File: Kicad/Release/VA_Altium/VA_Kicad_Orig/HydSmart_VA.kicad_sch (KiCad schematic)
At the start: 0 parts

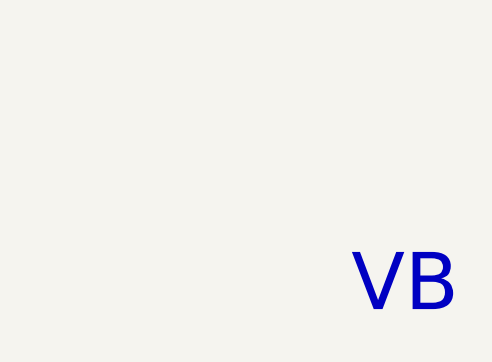
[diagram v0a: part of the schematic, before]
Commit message: VB changes start. Updated regulator and added test points
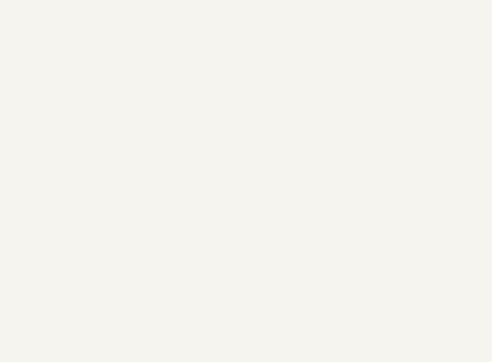
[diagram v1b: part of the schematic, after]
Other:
- note removed: "VB"
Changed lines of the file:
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@@
 	(generator_version "9.0")
 	(paper "A4")
-	(text "VB\n"
-		(exclude_from_sim no)
-		(at 226.06 173.736 0)
-		(effects
-			(font
-				(size 6.35 6.35)
-			)
-		)
-	)
 	(wire
 		(pts
